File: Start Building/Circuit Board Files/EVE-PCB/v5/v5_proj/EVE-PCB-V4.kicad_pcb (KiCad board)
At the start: 4 copper layers, 184.2 x 81.5 mm, 240 parts, among them J1 PJ-102AH, J2 2x20 Male Header, J3 1725669, J4 2x20 Male Header, J5 Conn_02x03_Odd_Even, J6 Conn_02x18_Odd_Even, J7 Conn_02x22_Odd_Even, Q1 UA7805CKCT, Q10 DMN6140LQ-7, Q11 DMN6140LQ-7, Q12 DMN6140LQ-7, Q13 DMN6140LQ-7, Q14 DMN6140LQ-7, Q15 DMN6140LQ-7, Q16 DMN6140LQ-7, Q17 DMN6140LQ-7, Q18 DMN6140LQ-7, Q19 DMN6140LQ-7, Q2 DMN6140LQ-7, Q20 DMN6140LQ-7, Q21 DMN6140LQ-7, Q22 DMN6140LQ-7, Q23 DMN6140LQ-7, Q24 DMN6140LQ-7, Q25 DMN6140LQ-7, Q26 DMN6140LQ-7, Q27 DMN6140LQ-7, Q28 DMN6140LQ-7, Q29 DMN6140LQ-7, Q3 DMN6140LQ-7, Q30 DMN6140LQ-7, Q31 DMN6140LQ-7, Q32 DMN6140LQ-7, Q4 DMN6140LQ-7, Q5 DMN6140LQ-7, Q6 DMN6140LQ-7, Q7 DMN6140LQ-7, Q8 DMN6140LQ-7, Q9 DMN6140LQ-7, U1 PCA9685PW, U10 INA219AxDCN, U11 INA219AxDCN, U12 AD5242, U13 AD5242, U14 PCA9685PW, U15 INA219AxDCN, U16 INA219AxDCN, U17 TLV4314IPWR, U18 AD5254 - 50K, U19 AD5254 - 50K, U2 ADS1115IDGSR, U20 AD5254 - 50K, U21 AD5254 - 50K, U22 TCA9548APWR, U23 TPS92511DDAR, U24 TPS92511DDAR, U25 TPS92511DDAR, U26 TPS92511DDAR, U27 ADS1115IDGSR, U28 TPS92511DDAR, U29 TPS92511DDAR, U3 TLV4314IPWR, U30 TPS92511DDAR, U31 TPS92511DDAR, U4 TLV4314IPWR, U5 MCP1501-10E/SN, U6 TLV4314IPWR, U7 PCA9685PW, U8 AD5242, U9 AD5242

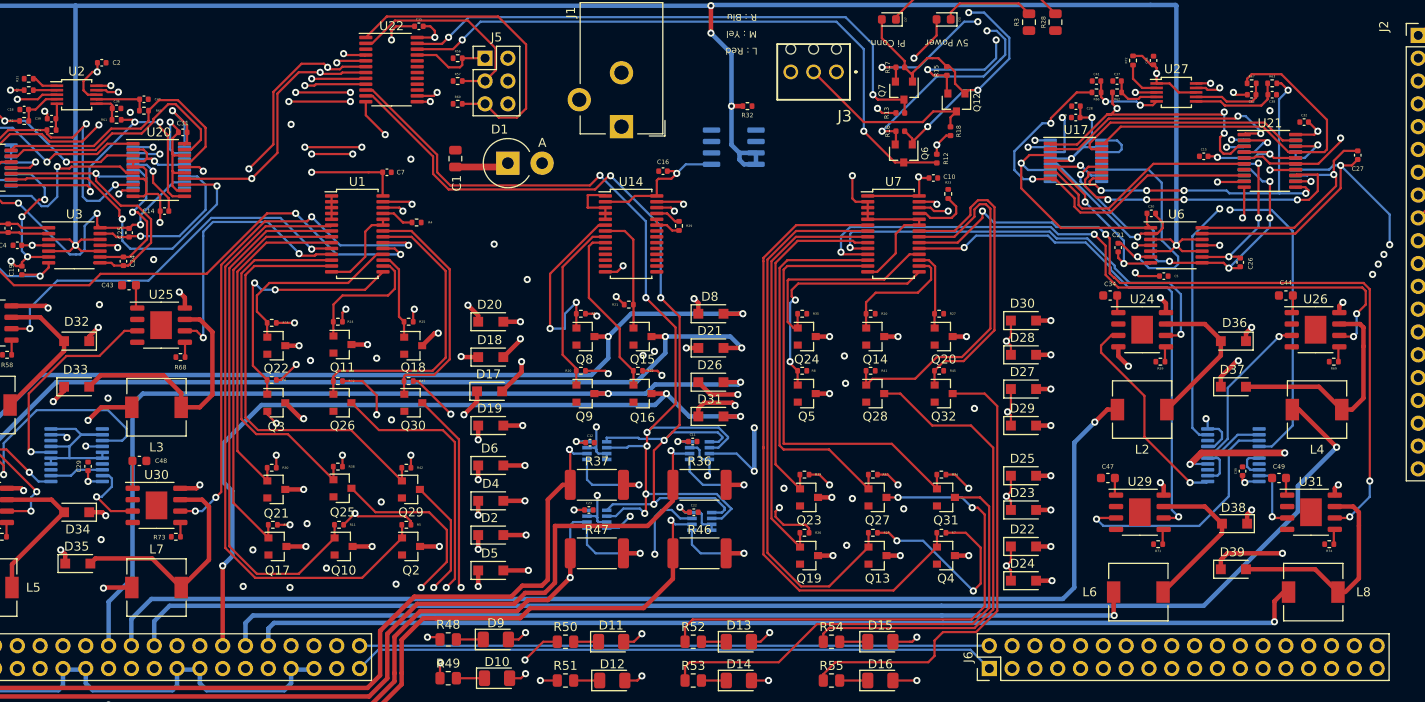
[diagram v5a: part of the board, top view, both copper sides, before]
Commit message: PCBv5 redesign current sensing
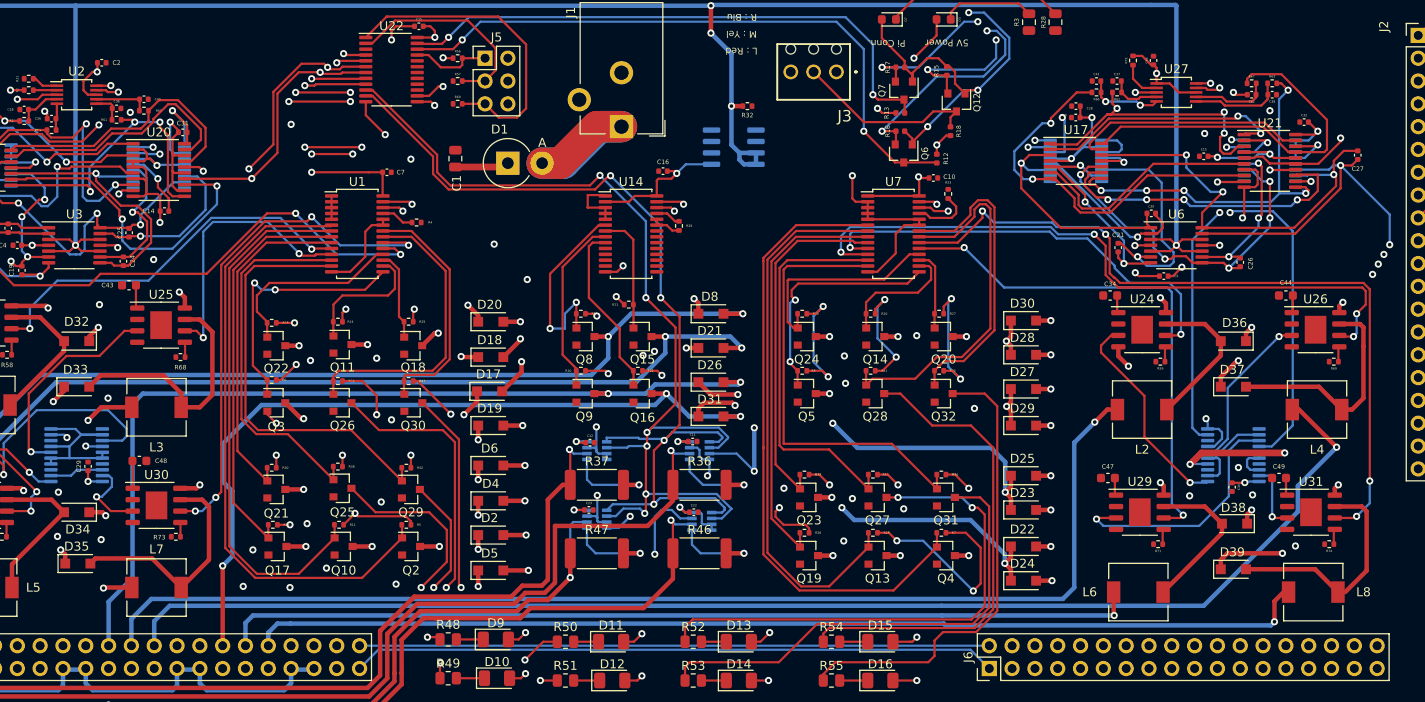
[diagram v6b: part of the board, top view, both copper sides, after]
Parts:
- moved C30 2.13 mm to (209.1, 84.1), turned to 90 degrees
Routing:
- net +5V: track 329.2 -> 380.5 mm, vias 80 -> 86
- net +12V: track 92.1 -> 138.1 mm, vias 20 -> 22
- net Net-(D1-Pad2): track 0.00 -> 42.1 mm
- net GND: track 281.6 -> 304.4 mm, vias 63 -> 74
- net /AVF42: track 27.2 -> 48.2 mm, vias 1 -> 3
- net /LED42_CCNEG: track 24.6 -> 25.8 mm
- net /ALP41: track 41.9 -> 43.1 mm
- net /SCL-ADC: track 146.1 -> 147.4 mm
- net /PD32_NEG: track 253.5 -> 252.4 mm
- net /LED41_PWM: track 58.5 -> 57.9 mm
- net /SDA-50KPOT: track 221.5 -> 220.9 mm
- net /APOT41: track 34.4 -> 35.0 mm
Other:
- net class mainpow added: clearance 0.3, trace_width 3.5, via_dia 0.8, via_drill 0.4

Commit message: Updates to PCB v5
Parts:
- removed U16: INA219AxDCN, Package_TO_SOT_SMD:SOT-23-8
- added C50: 1μF, Capacitor_SMD:C_0805_2012Metric, F.Cu at (149.1, 93.7)
- added C51: 0.1μF, Capacitor_SMD:C_0402_1005Metric, F.Cu at (147.3, 80.3)
- added C52: 0.1μF, Capacitor_SMD:C_0402_1005Metric, F.Cu at (144.0, 91.9)
- added C54: 0.1μF, Capacitor_SMD:C_0402_1005Metric, F.Cu at (154.2, 91.7)
- added R75: 750KΩ, Resistor_SMD:R_0603_1608Metric, F.Cu at (140.7, 84.6)
- added R76: 750KΩ, Resistor_SMD:R_0603_1608Metric, F.Cu at (153.2, 84.3)
- added R77: 750KΩ, Resistor_SMD:R_0603_1608Metric, F.Cu at (141.2, 95.5)
- added R78: 750KΩ, Resistor_SMD:R_0603_1608Metric, F.Cu at (152.4, 95.2)
- added U32: INA219AxDCN, Package_TO_SOT_SMD:SOT-23-8, F.Cu at (150.6, 90.2)
- C11, C12, C23: value 0.1μF -> 1μF; footprint Capacitor_SMD:C_0402_1005Metric -> Capacitor_SMD:C_0805_2012Metric
- R36, R37, R46, R47: value 0.4Ω -> 2.15Ω; footprint Resistor_SMD:R_2512_6332Metric -> Resistor_SMD:R_1206_3216Metric
- U10, U11, U15: moved to F.Cu
- moved C12 12.7 mm to (149.9, 82.8)
- moved U10 12.5 mm to (137.4, 79.5), turned to 90 degrees
- moved C11 12.4 mm to (137.4, 83.1)
- moved C22 11.0 mm to (140.5, 80.3), turned to 90 degrees
- moved U15 9.92 mm to (140.5, 90.2), turned to 90 degrees
- moved C23 7.17 mm to (138.4, 93.7)
- moved U11 6.61 mm to (145.0, 79.8), turned to 90 degrees
- moved R46 5.24 mm to (147.8, 96.3)
- moved R47 5.06 mm to (136.9, 96.3)
- moved R37 2.90 mm to (136.1, 85.6)
- moved R36 2.34 mm to (148.1, 85.3)
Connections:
- C11 pad 1: +5V -> /FAN1_POS
- C11 pad 2: GND -> /FILT_FAN1
- C12 pad 1: +5V -> /FAN2_POS
- C12 pad 2: GND -> /FILT_FAN2
- C23 pad 1: +5V -> /FAN3_POS
- C23 pad 2: GND -> /FILT_FAN3
- U10 pad 1: +12V -> /FILT_FAN1
- U10 pad 2: /FAN2_POS -> /FAN1_POS
- U10 pad 7: +5V -> GND
- U11 pad 1: +12V -> /FILT_FAN2
- U11 pad 2: /FAN1_POS -> /FAN2_POS
- U11 pad 7: GND -> +5V
- U15 pad 1: +12V -> /FILT_FAN3
- U15 pad 2: /FAN4_POS -> /FAN3_POS
- U15 pad 7: +5V -> GND
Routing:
- net +12V: track 138.1 -> 113.0 mm
- net /FILT_FAN2: track 0.00 -> 12.5 mm
- net /SCL-CUR: track 106.0 -> 116.0 mm, vias 4 -> 6
- net /FILT_FAN1: track 0.00 -> 6.27 mm
- net GND: track 304.4 -> 309.7 mm, vias 74 -> 75
- net /FILT_FAN4: track 0.00 -> 5.27 mm
- net /FILT_FAN3: track 0.00 -> 5.15 mm
- net +5V: track 380.5 -> 376.1 mm, vias 86 -> 83
- net /FAN2_POS: track 108.8 -> 112.9 mm, vias 2 -> 1
- net /SDA-CUR: track 109.1 -> 113.3 mm, vias 6 -> 4
- net /FAN3_POS: track 74.8 -> 72.6 mm, vias 2 -> 1
- net /FAN4_POS: track 73.4 -> 72.2 mm, vias 2 -> 1
- net /FAN1_POS: track 102.1 -> 102.4 mm, vias 1 -> 0
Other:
- net class fan_pos added: clearance 0.3, trace_width 0.5, via_dia 0.8, via_drill 0.4
- board text added: "Designed by Vishhvaan"
- board text added: "EVE"
- board text added: "JLCJLCJLCJLC"
- board text added: "v5"
